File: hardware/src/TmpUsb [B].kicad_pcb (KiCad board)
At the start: 2 copper layers, 25 x 17 mm, 17 parts, among them P1 48037-2200, U1 PIC18F26J50

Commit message: Updating footprints and net names
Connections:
- net PGC renamed ICSP_PGC
- net PGD renamed ICSP_PGD

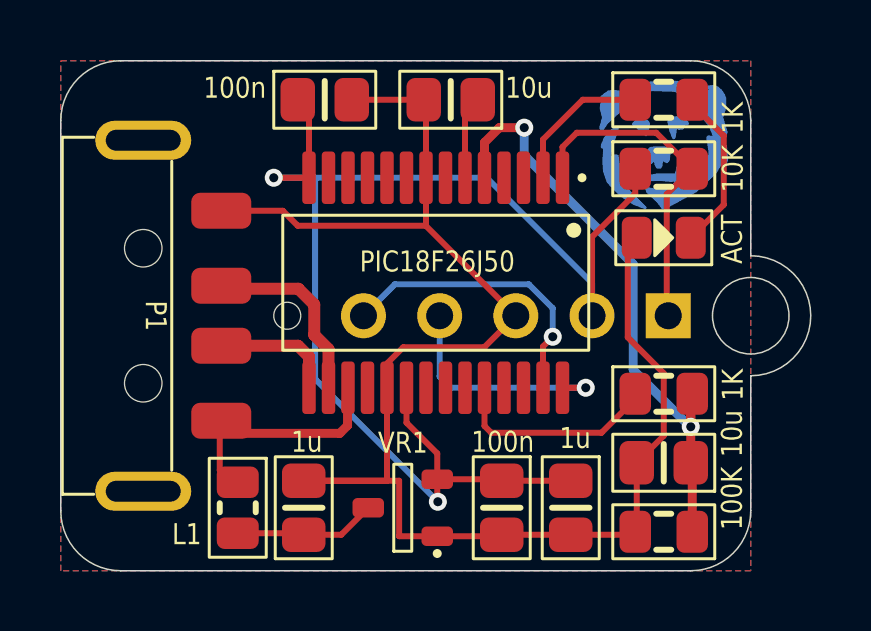
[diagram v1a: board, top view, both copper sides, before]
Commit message: Moved diode to center
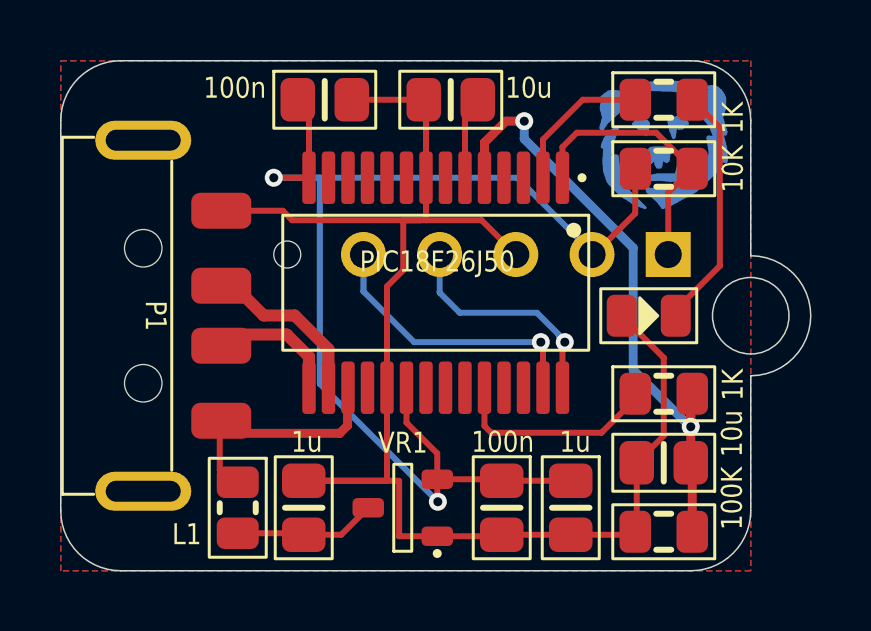
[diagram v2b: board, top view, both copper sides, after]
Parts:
- moved DS1 2.65 mm to (39.6, 28.5)
- moved ? 2.04 mm to (33.9, 26.5)
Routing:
- net GND: track 53.8 -> 49.5 mm
- net +3.3V: track 44.2 -> 40.8 mm
- net LED': track 5.34 -> 8.19 mm
- net ICSP_VPP: track 10.8 -> 8.83 mm
- net USB_D+: track 5.84 -> 5.24 mm
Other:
- board text added: "TmpUsb B2328"
- board text removed: "TmpUsb B2327"

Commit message: Pogo ICSP has copper exposed only on one side
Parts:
- ?: value J ICSP PIC Pogo (6w) -> J ICSP PIC Pogo (~{6}w); footprint Medo64-THD:J ICSP PIC Pogo (6w) -> Medo64-THD:J ICSP PIC Pogo (6*w)
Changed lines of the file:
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@@
       (stroke (width 0.1) (type solid)) (fill solid) (layer "B.Mask"))
   )
-  (footprint "Medo64-THD:J ICSP PIC Pogo (6w)" (layer "B.Cu")
+  (footprint "Medo64-THD:J ICSP PIC Pogo (6*w)" (layer "B.Cu")
     (at 33.9 26.459 180)
     (attr smd)
@@
         (effects (font (size 0.7 0.6) (thickness 0.1)) (justify bottom mirror))
     )
-    (fp_text value "J ICSP PIC Pogo (6w)" (at 0 -1.47 unlocked) (layer "B.Fab") hide
+    (fp_text value "J ICSP PIC Pogo (~{6}w)" (at 0 -1.47 unlocked) (layer "B.Fab") hide
         (effects (font (size 0.7 0.6) (thickness 0.1) bold) (justify top mirror))
+    )
+    (fp_text user "Vdd" (at -3.81 1.07 unlocked) (layer "User.7")
+        (effects (font (size 0.13 0.07) (thickness 0.014) bold) (justify top))
+    )
+    (fp_text user "PGC" (at 1.27 1.07 unlocked) (layer "User.7")
+        (effects (font (size 0.13 0.07) (thickness 0.01)) (justify top))
+    )
+    (fp_text user "PGD" (at 3.81 1.07 unlocked) (layer "User.7")
+        (effects (font (size 0.13 0.07) (thickness 0.01)) (justify top))
+    )
+    (fp_text user "Vpp" (at -6.35 1.07 unlocked) (layer "User.7")
+        (effects (font (size 0.13 0.07) (thickness 0.014) bold) (justify top))
     )
     (fp_text user "GND" (at -1.27 1.07 unlocked) (layer "User.7")
         (effects (font (size 0.13 0.07) (thickness 0.014) bold) (justify top))
     )
-    (fp_text user "Vdd" (at -3.81 1.07 unlocked) (layer "User.7")
-        (effects (font (size 0.13 0.07) (thickness 0.014) bold) (justify top))
-    )
-    (fp_text user "Vpp" (at -6.35 1.07 unlocked) (layer "User.7")
-        (effects (font (size 0.13 0.07) (thickness 0.014) bold) (justify top))
-    )
-    (fp_text user "PGD" (at 3.81 1.07 unlocked) (layer "User.7")
-        (effects (font (size 0.13 0.07) (thickness 0.01)) (justify top))
-    )
-    (fp_text user "PGC" (at 1.27 1.07 unlocked) (layer "User.7")
-        (effects (font (size 0.13 0.07) (thickness 0.01)) (justify top))
-    )
     (fp_rect (start -7.62 1.27) (end 7.62 -1.27)
       (stroke (width 0.2) (type default)) (fill none) (layer "B.SilkS"))
     (pad "" np_thru_hole circle (at 6.35 0 180) (size 0.9 0.9) (drill 0.9) (layers "F&B.Cu" "*.Mask"))
-    (pad "1" thru_hole rect (at -6.35 0 180) (size 1.5 1.5) (drill 0.9) (layers "*.Cu" "*.Mask")
+    (pad "1" thru_hole rect (at -6.35 0 180) (size 1.5 1.5) (drill 0.9) (layers "*.Cu" "B.Mask")
       (net 6 "ICSP_VPP"))
-    (pad "2" thru_hole circle (at -3.81 0 180) (size 1.5 1.5) (drill 0.9) (layers "*.Cu" "*.Mask")
+    (pad "2" thru_hole circle (at -3.81 0 180) (size 1.5 1.5) (drill 0.9) (layers "*.Cu" "B.Mask")
       (net 11 "+3.3V"))
-    (pad "3" thru_hole circle (at -1.27 0 180) (size 1.5 1.5) (drill 0.9) (layers "*.Cu" "*.Mask")
+    (pad "3" thru_hole circle (at -1.27 0 180) (size 1.5 1.5) (drill 0.9) (layers "*.Cu" "B.Mask")
       (net 3 "GND"))
-    (pad "4" thru_hole circle (at 1.27 0 180) (size 1.5 1.5) (drill 0.9) (layers "*.Cu" "*.Mask")
+    (pad "4" thru_hole circle (at 1.27 0 180) (size 1.5 1.5) (drill 0.9) (layers "*.Cu" "B.Mask")
       (net 13 "ICSP_PGD"))
-    (pad "5" thru_hole circle (at 3.81 0 180) (size 1.5 1.5) (drill 0.9) (layers "*.Cu" "*.Mask")
+    (pad "5" thru_hole circle (at 3.81 0 180) (size 1.5 1.5) (drill 0.9) (layers "*.Cu" "B.Mask")
       (net 14 "ICSP_PGC"))
   )
